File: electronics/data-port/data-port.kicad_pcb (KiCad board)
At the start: 2 copper layers, 40 x 17 mm, 9 parts, among them J1 DATA, J2 LEAD, U1 USBLC6-2SC6

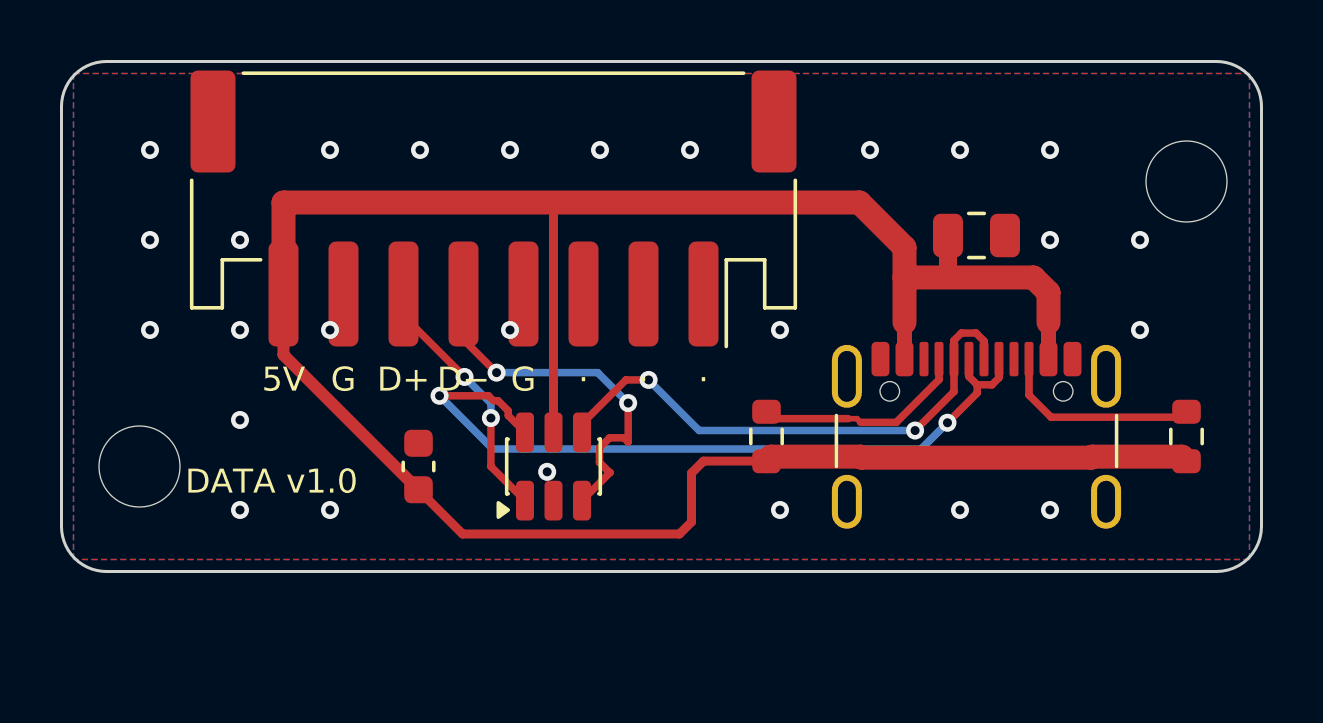
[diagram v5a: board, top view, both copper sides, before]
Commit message: Boards: labelled bottom test pads; hub dVdT 100 nF, 50 ms FLT blank
Eve's DFT rule on the four boards this session owns: bare pads on the
bottom, named on B.SilkS, out of the BOM and the CPL (no part, no
assembly fee).  Supply pads 1.5 mm, signal pads 1.0 mm (new catalog
entry "testpad1"), all more than 2 mm from any THT pad or hole
(closest: 4.7 mm, the pod's TP4).  Positions are fixed in design.py,
so they stay put across revisions.

- bay node, 17: TX, RX, 3V3, GND by the module (kept), then EN, IO0,
  FLT (DUT_FLT_N), ALRT (INA_ALERT_N), SDA, SCL and a second GND;
  a supply row along the bottom edge: GND, VIN, 5V, 3V3, DUT 5V,
  CAM 5V
- power hub, 20: TX, RX, 3V3, GND, 5V, VRACK, GND (kept), then EN,
  IO0, the CH224A's PD SDA/SCL, each row's FLT and IMON (A-D) and a
  third GND in the middle
- camera pod, 4: GND, 5V, 3V3 and a second GND at the far end
- DATA port, 2: GND and 5V (VBUS, through a via under its track)

Hub, as the datasheet audit's U1 answer asks (TPS2660 Fig. 55 at
85 C: 8-10 ms at 21 W fails the 47 nF worst start, 33 ms at 14 W
covers 100 nF): C21-C24 dVdT 47 nF -> 100 nF, so a row's soft start
is 16-22 ms and dissipates about 7-9 W typical, 14 W worst, for
19-24 ms; the firmware's HUB_ROW_FLT_BLANK_MS goes 25 -> 50 ms to
cover it (worst case 39 ms).  docs/power.md, the audit row and the
hub notes say so.

Routing fallout: J1's A12/B1 GND now leaves through one drawn 0.5 mm
via so the automatic fan-out can't cut the VRACK pour off A9/B4; the
pod's LDO tab zones are exclusive so tracks no longer split them.

All four rerouted, tidied and checked: ERC 0, DRC 0, unconnected 0,
parity 0.  Gerbers, renders, schematics, viewer GLBs, the JLC
snapshot lines and the rack BOM regenerated.

Co-Authored-By: Claude Opus 5.5 <noreply@anthropic.com>
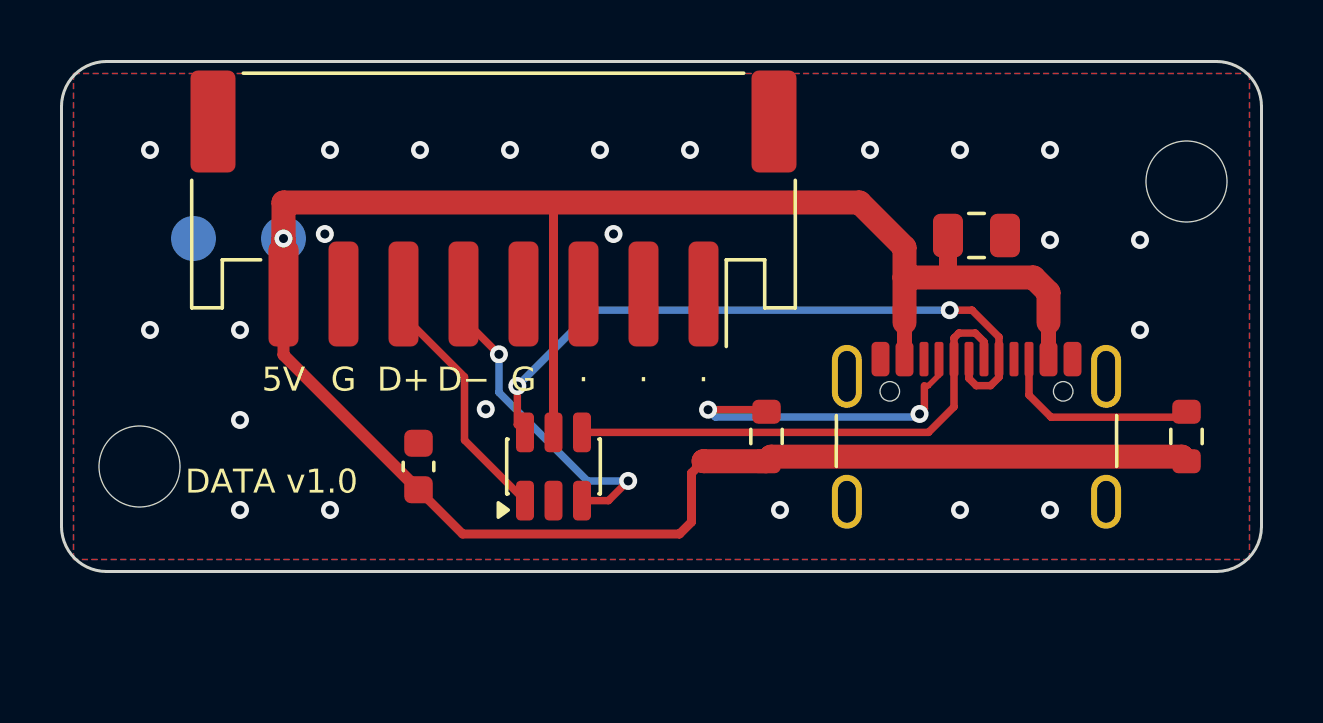
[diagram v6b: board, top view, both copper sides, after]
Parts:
- added TP1: GND, TestPoint:TestPoint_Pad_D1.5mm, B.Cu at (4.40, 5.90)
- added TP2: VBUS, TestPoint:TestPoint_Pad_D1.5mm, B.Cu at (7.40, 5.90)
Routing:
- net /Port/CC1: track 7.17 -> 11.3 mm, vias 0 -> 2
- net /Port/CONN_DP: track 25.6 -> 22.3 mm
- net /Port/VBUS: track 95.1 -> 98.3 mm, vias 0 -> 1
- net /Port/LEAD_DN: track 12.6 -> 11.1 mm
- net /Port/CONN_DN: track 18.0 -> 16.8 mm, vias 2 -> 0
- net GND: vias 26 -> 23
- net /Port/LEAD_DP: vias 2 -> 0
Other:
- board text added: "GND"

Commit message: DATA port: GND vias by the lead's GND pins and the ESD (DP-2)
The kicad-happy review's DP-2: J2.4 and J2.7 carry the whole DUT return
(up to 1.52 A), and the F.Cu island around them went down to the B.Cu
pour through a single 0.3 mm via.  Each pin now has a drawn 0.5 mm stub
from its pad to a GND via beside the pad's end, at (8.65, 9.9) and
(14.6, 10.0).

The via by pin 4 sat on D-'s (LEAD_DN's), so Freerouting re-routed D-
alone: 13.0 mm instead of 11.1, still two vias.  D+ (8.6 mm) is
unchanged.  Its first attempt walled the ESD's GND pin (U1.2) off the
F.Cu pour, so U1.2 also gets its own via, under the part between its
rows: the short GND the USBLC6 wants.

Every other track and via is main's, untouched.  Same stitching.
ERC 0, DRC 0, unconnected 0, parity 0.

Co-Authored-By: Claude Opus 5.5 <noreply@anthropic.com>
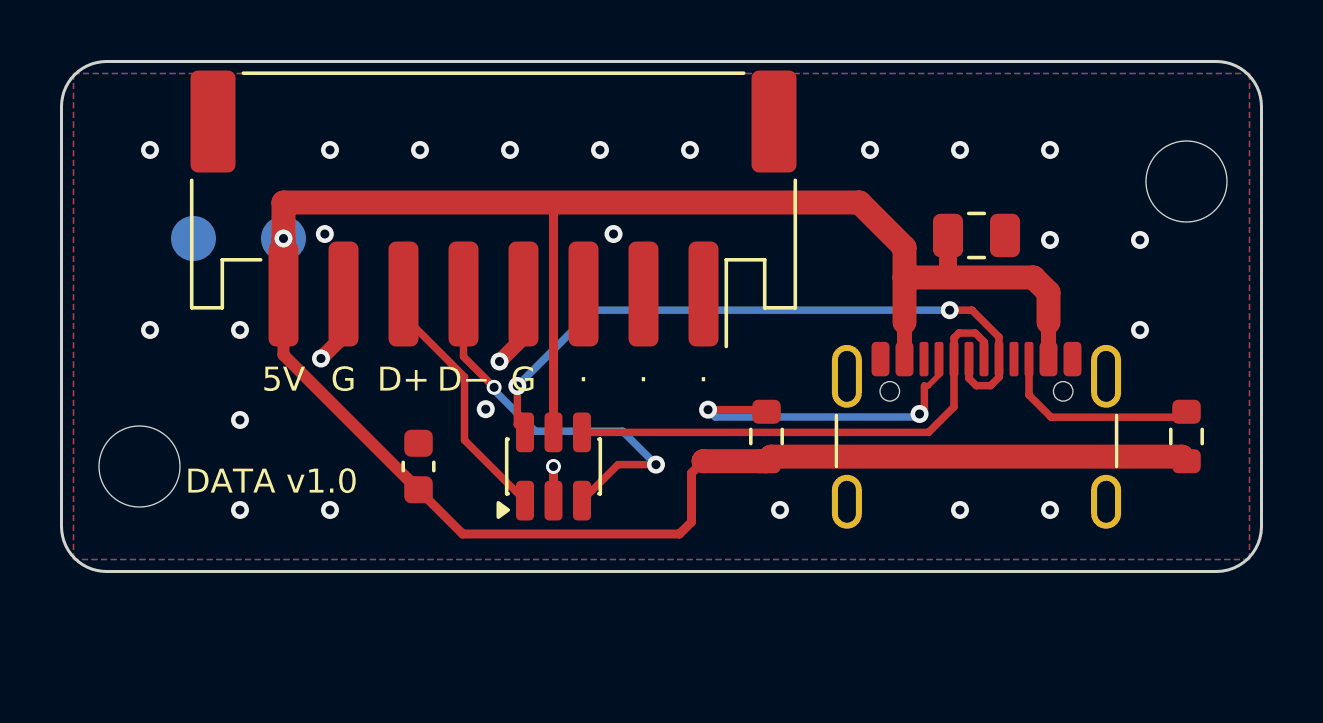
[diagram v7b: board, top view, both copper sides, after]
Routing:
- net GND: track 0.00 -> 6.18 mm, vias 23 -> 26
- net /Port/LEAD_DN: track 11.1 -> 13.0 mm

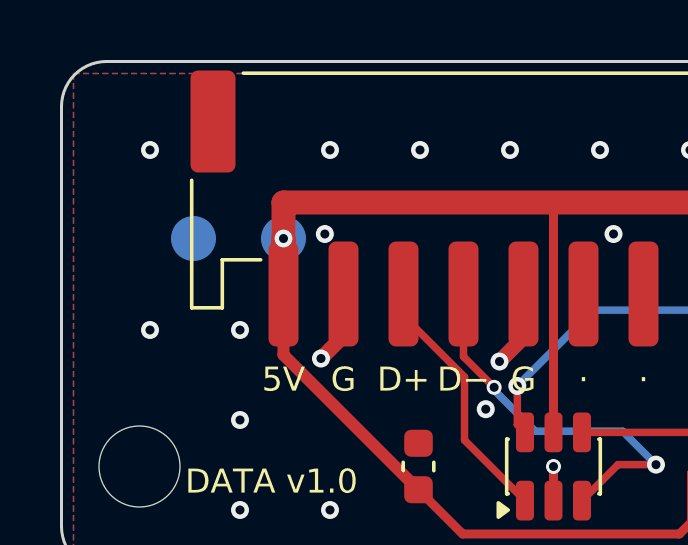
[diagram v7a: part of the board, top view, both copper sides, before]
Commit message: DATA port: TP2's via off J2.8's pad (DP-3)
The kicad-happy review's DP-3: TP2 (VBUS, bottom) joins the top-side
VBUS track through a via in its own pad, and at y 5.9 that via's ring
overlapped J2.8's pad on top by 0.2 mm.  J2.8 is the lead's VBUS pin,
with full paste, so the pin's solder could drain down the via.  The two
bottom test pads, the via and their B.SilkS labels move up 0.55 mm, to
y 5.35 (TP_Y): 0.35 mm clear of J2.8, still under the VBUS track.

No routing change: every track and via but that one is the previous
commit's.  ERC 0, DRC 0, unconnected 0, parity 0.

Co-Authored-By: Claude Opus 5.5 <noreply@anthropic.com>
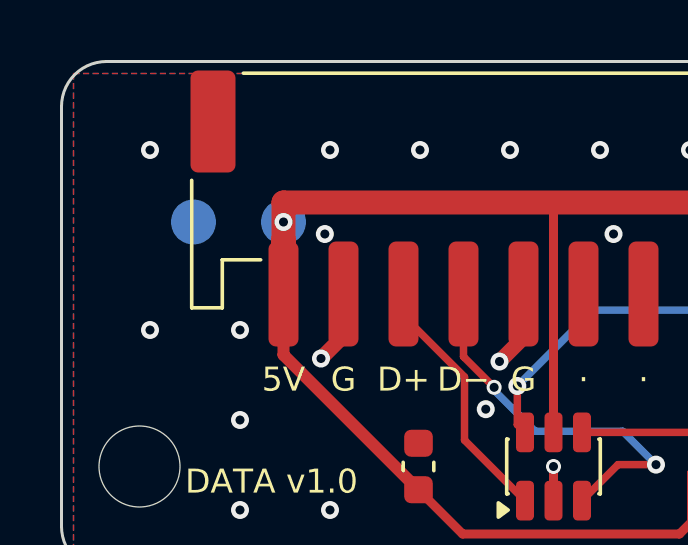
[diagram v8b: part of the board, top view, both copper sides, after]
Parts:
- moved TP1 0.55 mm to (4.40, 5.35)
- moved TP2 0.55 mm to (7.40, 5.35)
